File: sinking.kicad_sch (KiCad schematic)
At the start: 11 parts, among them Q1 Q_NPN_BCE, U1 LTV-817, U2 V7805-1000, U3 INA219AxD

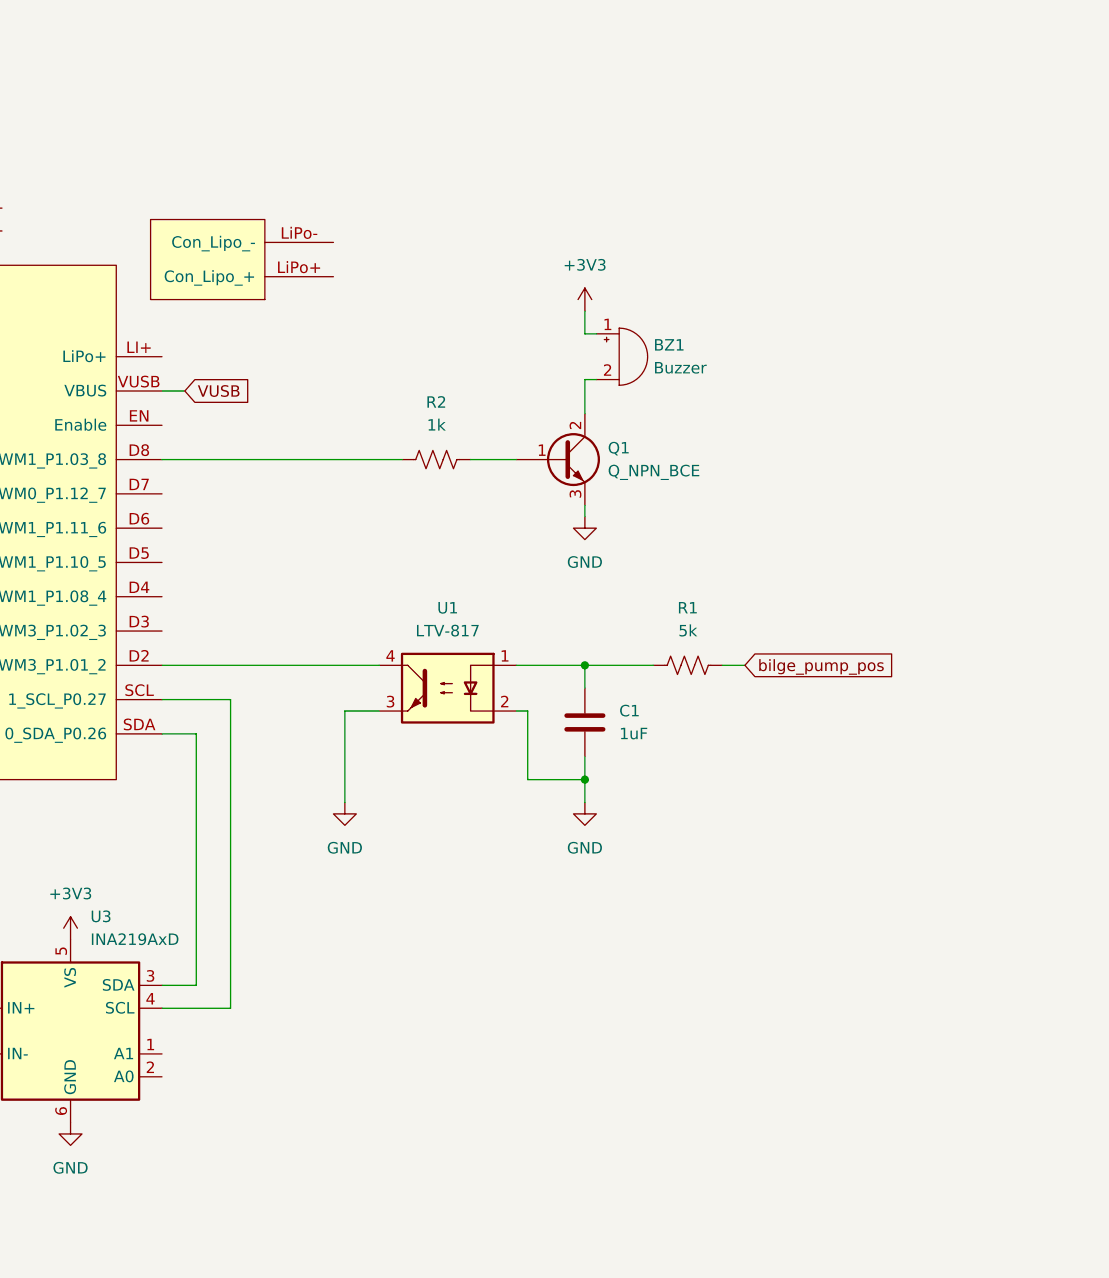
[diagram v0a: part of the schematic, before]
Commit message: improve pump input filter. add simulation
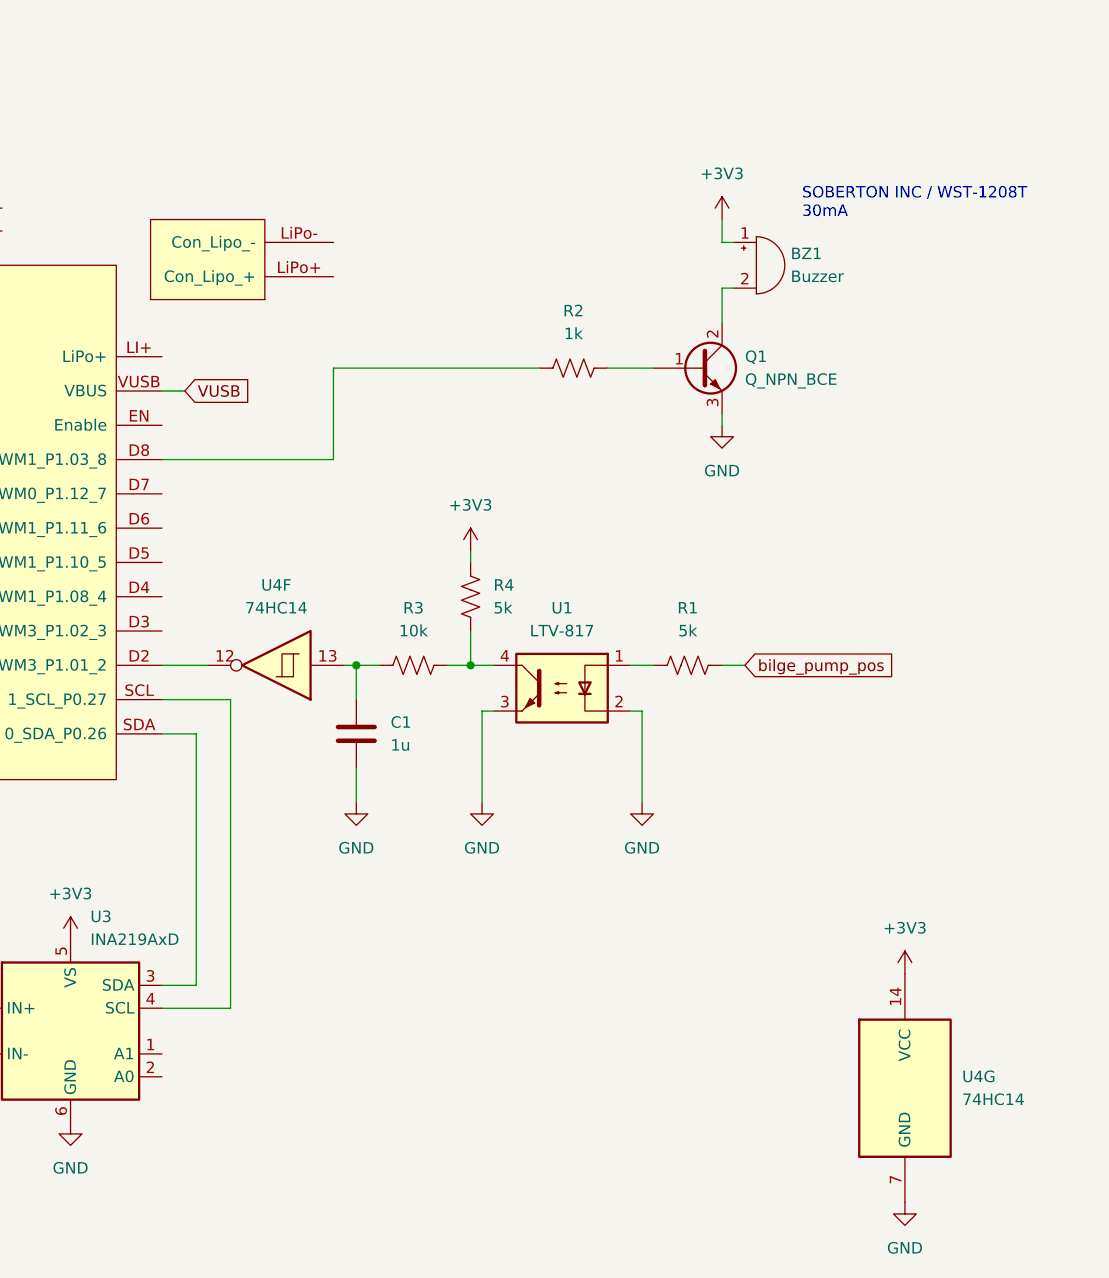
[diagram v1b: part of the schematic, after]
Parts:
- added R3: 10k, Resistor_SMD:R_0805_2012Metric, symbol Device:R_US
- added R4: 5k, Resistor_SMD:R_0805_2012Metric, symbol Device:R_US
- added U4: 74HC14, Package_DIP:DIP-14_W7.62mm, symbol 74xx:74HC14
- BZ1: footprint (none) -> Buzzer_Beeper:MagneticBuzzer_ProSignal_ABI-009-RC
- C1: value 1uF -> 1u; footprint (none) -> Capacitor_SMD:C_0805_2012Metric
- C2, C3: footprint (none) -> Capacitor_SMD:C_1210_3225Metric
- Q1: footprint (none) -> Package_TO_SOT_SMD:SOT-23
- R1, R2: footprint (none) -> Resistor_SMD:R_0805_2012Metric
- U2: footprint V7805-1000:CONV_V7805-1000 -> libs:CONV_V7805-1000
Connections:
- net +3V3: now also R4.2, U4.14 (VCC)
- net GND: now also U4.7 (GND)
- net at R1.1, U1.1: no longer C1.1
- net at U1.4: now also R3.2, R4.1; no longer A1.D2 (SDA1_UART1_RTS_SPI1_SCK_PWM3_P1.01_2)
- new net: C1.1, R3.1, U4.13
- new net: A1.D2 (SDA1_UART1_RTS_SPI1_SCK_PWM3_P1.01_2), U4.12
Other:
- note added: "SOBERTON INC / WST-1208T 30mA"
- moved on the sheet: BZ1, Q1, R2, U1

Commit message: first layout
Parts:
- removed C1: 1u, Capacitor_SMD:C_0805_2012Metric, symbol Device:C
- removed R1, R4: 5k, Resistor_SMD:R_0805_2012Metric, symbol Device:R_US
- removed R3: 10k, Resistor_SMD:R_0805_2012Metric, symbol Device:R_US
- removed U1: LTV-817, Package_DIP:DIP-4_W7.62mm, symbol Isolator:LTV-817
- removed U3: INA219AxD, Package_SO:SOIC-8_3.9x4.9mm_P1.27mm, symbol Sensor_Energy:INA219AxD
- removed U4: 74HC14, Package_DIP:DIP-14_W7.62mm, symbol 74xx:74HC14
- added C12, C13: 1u, Capacitor_SMD:C_0805_2012Metric, symbol Device:C
- added D1: PMEG2005, Package_TO_SOT_SMD:SOT-23_Handsoldering, symbol Diode:BAT54C
- added JP1: SolderJumper_3_Open, Jumper:SolderJumper-3_P2.0mm_Open_TrianglePad1.0x1.5mm, symbol Jumper:SolderJumper_3_Open
- added R19, R20: 10k, Resistor_SMD:R_0805_2012Metric, symbol Device:R_US
- added R24: 0, Resistor_SMD:R_1210_3225Metric_Pad1.30x2.65mm_HandSolder, symbol Device:R_US
- added U5: TPS7A2033PDBVR, Package_TO_SOT_SMD:SOT-23-5, symbol Regulator_Linear:TPS7A0533PDBV
- A1: footprint boron:Boron -> libs:Boron; symbol particle:Particle_Boron -> particle_lib:Particle_Boron
- renumbered C2 to C1, C3 to C2, R2 to R1, U2 to U1
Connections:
- net +3V3: now also R19.2, R20.2; no longer BZ1.1 (+)
- net GND: now also C12.2, C13.2, U5.2 (GND)
- net VUSB: now also D1.2
- net buzzer -: now reaches BZ1.2 (-), Q1.2 (C)
- net water_sense_sig: now reaches A1.A0 (19_P0.03_PWM2_ADC0)
- net input_filter/out: now reaches A1.D2 (SDA1_UART1_RTS_SPI1_SCK_PWM3_P1.01_2)
- net input_filter/out: now also JP1.1 (A)
- net at A1.D3 (SCL1_UART1_CTS_SPI1_MOSI_PWM3_P1.02_3): now also JP1.2 (C)
- net input_filter1/out: now reaches A1.D4 (UART2_TX_SPI1_MISO_PWM1_P1.08_4)
- net input_filter1/out: now also JP1.3 (B)
- net input_filter2/out: now reaches A1.D5 (UART2_RX_PWM1_P1.10_5)
- net input_filter3/out: now reaches A1.D6 (UART2_CTS_PWM1_P1.11_6)
- net at A1.LI+ (LiPo+): now also D1.1
- net SCL: now reaches A1.SCL (1_SCL_P0.27)
- net SCL: now also R19.1
- net SDA: now reaches A1.SDA (0_SDA_P0.26)
- net SDA: now also R20.1
- net +12V: no longer names the net of C1.1, U1.1 (+VIN)
- net +12V: now also R24.2
- new net: C12.1, D1.3, U5.1 (IN), U5.3 (EN)
- new net +12V_IN_-: R24.1
- new net buzzer +: BZ1.1 (+), C13.1, U5.5 (OUT)
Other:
- added sheet Connectors (connectors.kicad_sch)
- added sheet INA219 (INA219.kicad_sch)
- added sheet INA219_2 (INA219.kicad_sch)
- added sheet input_filter (input_filter.kicad_sch)
- added sheet input_filter1 (input_filter.kicad_sch)
- added sheet input_filter2 (input_filter.kicad_sch)
- added sheet input_filter3 (input_filter.kicad_sch)
- added sheet scrapyard (scrapyard.kicad_sch)
- note added: "series resistor for supply noise filtering"
- moved on the sheet: BZ1, C1, C2, Q1, R1, U1

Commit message: add status led, etc.
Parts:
- added D2: CTL0805FRD1T, LED_SMD:LED_0805_2012Metric_Pad1.15x1.40mm_HandSolder, symbol Device:LED
- added D3: LED, LED_SMD:LED_0805_2012Metric_Pad1.15x1.40mm_HandSolder, symbol Device:LED
- added R32, R33: 330, Resistor_SMD:R_0805_2012Metric, symbol Device:R_US
- Q1: footprint Package_TO_SOT_SMD:SOT-23 -> Package_TO_SOT_SMD:SOT-23_Handsoldering
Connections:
- net GND: now also D3.1 (K)
- net Vin: now reaches C1.1, R24.2, U1.1 (+VIN)
- net at A1.A5 (14_P0.31_PWM3_ADC5_SPI_SS): now also R33.2
- net +12V_IN_- renamed bat_sense_-
- net buzzer + renamed buzzer_+
- net buzzer_+: now also R32.1
- net buzzer - renamed buzzer_-
- net buzzer_-: now also D2.1 (K)
- new net: D2.2 (A), R32.2
- new net: D3.2 (A), R33.1
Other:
- sheet Connectors renamed connectors
- moved on the sheet: BZ1, Q1
